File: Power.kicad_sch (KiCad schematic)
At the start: 54 parts, among them IC115 RC4558, IC116 RC4558, IC117 RC4558, IC118 L7805, IC121 1951A, IC135 74HC86, IC136 1951A, P1 Conn_01x02_Male, P3 Conn_01x02_Male

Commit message: PCE expansion port added with only relevant pins.
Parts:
- removed R120: 270, symbol Device:R
- added SPC-E: PCE-EXPANSION-CONN, symbol IFU-30:PCE-EXPANSION-CONN
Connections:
- net 8.5V: now also SPC-E.A11 (VIN), SPC-E.A14 (VIN)
- net GND: now also SPC-E.A21 (GNDA), SPC-E.B2 (CDD), SPC-E.C17 (GNDD), SPC-E.C2 (GNDA), SPC-E.C20 (GNDD), SPC-E.C8 (GNDD)
- net SPC-E_5V renamed PCE_5VOUT
- net PCE_5VOUT: now also SPC-E.A2 (VOUT), SPC-E.C21 (VOUT)
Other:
- moved on the sheet: C1, C103, C132, C133, C134, C15, C2, C3, C54, C55, C6, C7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

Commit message: All calculations added.
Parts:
- added IC114: TL072, symbol Amplifier_Operational:TL072
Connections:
- net 7.9V: now also IC114.8 (V+)
- net GND: now also IC114.4 (V-)
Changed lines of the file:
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@@
+    (stroke (width 0) (type default) (color 0 0 0 0))
+  )
+  (wire (pts (xy 329.565 238.125) (xy 329.565 239.395))
     (stroke (width 0) (type default) (color 0 0 0 0))
   )
@@
     (stroke (width 0) (type default) (color 0 0 0 0))
   )
+  (wire (pts (xy 329.565 222.25) (xy 321.945 222.25))
+    (stroke (width 0) (type default) (color 0 0 0 0))
+  )
   (wire (pts (xy 127 102.87) (xy 113.665 102.87))
     (stroke (width 0) (type default) (color 0 0 0 0))
@@
   )
   (wire (pts (xy 243.84 211.455) (xy 252.73 211.455))
+    (stroke (width 0) (type default) (color 0 0 0 0))
+  )
+  (wire (pts (xy 329.565 222.25) (xy 329.565 222.885))
     (stroke (width 0) (type default) (color 0 0 0 0))
   )
@@
   )
   (label "8.5V" (at 64.77 128.27 0)
+    (effects (font (size 1.27 1.27)) (justify left bottom))
+  )
+  (label "7.9V" (at 321.945 222.25 0)
     (effects (font (size 1.27 1.27)) (justify left bottom))
   )
@@
     (pin "1")
   )
+  (symbol (lib_id "Amplifier_Operational:TL072") (at 332.105 230.505 0) (unit 3)
+    (in_bom yes) (on_board yes) (fields_autoplaced)
+    (property "Reference" "IC114" (id 0) (at 330.2 229.6703 0)
+      (effects (font (size 1.27 1.27)) (justify left))
+    )
+    (property "Value" "TL072" (id 1) (at 330.2 232.2072 0)
+      (effects (font (size 1.27 1.27)) (justify left))
+    )
+    (property "Footprint" "" (id 2) (at 332.105 230.505 0)
+      (effects (font (size 1.27 1.27)) hide)
+    )
+    (property "Datasheet" "http://www.ti.com/lit/ds/symlink/tl071.pdf" (id 3) (at 332.105 230.505 0)
+      (effects (font (size 1.27 1.27)) hide)
+    )
+    (pin "1")
+    (pin "2")
+    (pin "3")
+    (pin "5")
+    (pin "6")
+    (pin "7")
+    (pin "4")
+    (pin "8")
+  )
   (symbol (lib_id "74xx:74HC86") (at 207.645 211.455 0) (unit 2)
     (in_bom yes) (on_board yes) (fields_autoplaced)
@@
       (effects (font (size 1.27 1.27)) hide)
     )
+    (pin "1")
+  )
+  (symbol (lib_id "power:GND") (at 329.565 239.395 0) (mirror y) (unit 1)
+    (in_bom yes) (on_board yes)
+    (property "Reference" "#PWR0102" (id 0) (at 329.565 245.745 0)
+      (effects (font (size 1.27 1.27)) hide)
+    )
+    (property "Value" "GND" (id 1) (at 329.565 243.84 0))
+    (property "Footprint" "" (id 2) (at 329.565 239.395 0)
+      (effects (font (size 1.27 1.27)) hide)
+    )
+    (property "Datasheet" "" (id 3) (at 329.565 239.395 0)
+      (effects (font (size 1.27 1.27)) hide)
+    )

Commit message: Documentation started.
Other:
- title: (none) -> NEC PC-Engine IFU-30
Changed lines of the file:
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@@
 (kicad_sch (version 20211123) (generator eeschema)
   (paper "A3")
+  (title_block
+    (title "NEC PC-Engine IFU-30")
+    (date "2022-10-27")
+    (rev "0.1")
+    (comment 1 "Author: Regis Galland")
+    (comment 2 "NEC IFU-30 PCB reverse engineered schematics")
+  )
   (junction (at 163.195 128.27) (diameter 0) (color 0 0 0 0)
   )

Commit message: Documentation update
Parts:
- ZD10: value D_Zener -> 5.1V
- ZD11: value D_Zener -> 8.2V
- renumbered SPC-E to SPC-E1
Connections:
- net 7.9V renamed 7.8V
- net VBIAS_3.95V renamed VBIAS_3.9V
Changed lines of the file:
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@@
     (effects (font (size 1.27 1.27)) (justify left bottom))
   )
-  (label "7.9V" (at 321.945 222.25 0)
+  (label "7.8V" (at 321.945 222.25 0)
     (effects (font (size 1.27 1.27)) (justify left bottom))
   )
@@
     (effects (font (size 1.27 1.27)) (justify left bottom))
   )
-  (label "VBIAS_3.95V" (at 168.91 105.41 0)
+  (label "VBIAS_3.9V" (at 168.91 105.41 0)
     (effects (font (size 1.27 1.27)) (justify left bottom))
   )
-  (label "7.9V" (at 100.33 89.535 0)
+  (label "7.8V" (at 100.33 89.535 0)
     (effects (font (size 1.27 1.27)) (justify left bottom))
   )
-  (hierarchical_label "7.9V" (shape output) (at 102.87 85.09 0)
+  (hierarchical_label "7.8V" (shape output) (at 102.87 85.09 0)
     (effects (font (size 1.27 1.27)) (justify left))
   )
@@
     (effects (font (size 1.27 1.27)) (justify left))
   )
-  (hierarchical_label "VBIAS_3.95V" (shape output) (at 200.025 105.41 0)
+  (hierarchical_label "VBIAS_3.9V" (shape output) (at 200.025 105.41 0)
     (effects (font (size 1.27 1.27)) (justify left))
   )
@@
     (pin "2")
   )
-  (symbol (lib_id "IFU-30:PCE-EXPANSION-CONN") (at 74.93 127 0) (unit 4)
-    (in_bom yes) (on_board yes)
-    (property "Reference" "SPC-E" (id 0) (at 90.17 121.2881 0))
-    (property "Value" "PCE-EXPANSION-CONN" (id 1) (at 90.17 123.825 0))
-    (property "Footprint" "" (id 2) (at 74.93 127 0)
-      (effects (font (size 1.27 1.27)) hide)
-    )
-    (property "Datasheet" "" (id 3) (at 74.93 127 0)
+  (symbol (lib_id "IFU-30:PCE-EXPANSION-CONN") (at 74.93 128.27 0) (unit 4)
+    (in_bom yes) (on_board yes)
+    (property "Reference" "SPC-E1" (id 0) (at 90.17 122.5581 0))
+    (property "Value" "PCE-EXPANSION-CONN" (id 1) (at 90.17 125.095 0))
+    (property "Footprint" "" (id 2) (at 74.93 128.27 0)
+      (effects (font (size 1.27 1.27)) hide)
+    )
+    (property "Datasheet" "" (id 3) (at 74.93 128.27 0)
       (effects (font (size 1.27 1.27)) hide)
     )
@@
     (pin "1")
   )
+  (symbol (lib_id "power:GND") (at 365.125 45.085 0) (unit 1)
+    (in_bom yes) (on_board yes) (fields_autoplaced)
+    (property "Reference" "#PWR0224" (id 0) (at 365.125 51.435 0)
+      (effects (font (size 1.27 1.27)) hide)
+    )
+    (property "Value" "GND" (id 1) (at 365.125 49.5284 0))
+    (property "Footprint" "" (id 2) (at 365.125 45.085 0)
+      (effects (font (size 1.27 1.27)) hide)
+    )
+    (property "Datasheet" "" (id 3) (at 365.125 45.085 0)
+      (effects (font (size 1.27 1.27)) hide)
+    )
+    (pin "1")
+  )
   (symbol (lib_id "power:GND") (at 360.045 147.32 90) (unit 1)
     (in_bom yes) (on_board yes) (fields_autoplaced)
@@
   (symbol (lib_id "Device:Q_PNP_ECB") (at 274.955 103.505 180) (unit 1)
     (in_bom yes) (on_board yes)
-    (property "Reference" "TR1" (id 0) (at 266.7031 95.885 90)
-      (effects (font (size 1.27 1.27)) (justify left))
-    )
-    (property "Value" "Q_PNP_ECB" (id 1) (at 269.24 95.885 90)
+    (property "Reference" "TR1" (id 0) (at 269.24 104.1369 0)
+      (effects (font (size 1.27 1.27)) (justify left))
+    )
+    (property "Value" "Q_PNP_ECB" (id 1) (at 269.24 101.6 0)
       (effects (font (size 1.27 1.27)) (justify left))
     )
@@
   (symbol (lib_id "Device:R") (at 309.245 52.705 0) (mirror x) (unit 1)
     (in_bom yes) (on_board yes)
-    (property "Reference" "R105" (id 0) (at 313.9608 52.705 90))
-    (property "Value" "820" (id 1) (at 311.785 52.705 90))
+    (property "Reference" "R105" (id 0) (at 313.69 51.1642 0))
+    (property "Value" "820" (id 1) (at 313.69 53.34 0))
     (property "Footprint" "" (id 2) (at 307.467 52.705 90)
       (effects (font (size 1.27 1.27)) hide)
@@
   (symbol (lib_id "Device:D_Zener") (at 266.065 162.56 0) (mirror x) (unit 1)
     (in_bom yes) (on_board yes)
-    (property "Reference" "ZD13" (id 0) (at 265.2303 164.592 90)
-      (effects (font (size 1.27 1.27)) (justify left))
-    )
-    (property "Value" "D_Zener" (id 1) (at 267.7672 164.592 90)
+    (property "Reference" "ZD13" (id 0) (at 262.255 158.75 0)
+      (effects (font (size 1.27 1.27)) (justify left))
+    )
+    (property "Value" "D_Zener" (id 1) (at 262.255 156.2131 0)
       (effects (font (size 1.27 1.27)) (justify left))
     )
@@
   (symbol (lib_id "Device:D") (at 309.245 41.91 270) (mirror x) (unit 1)
     (in_bom yes) (on_board yes)
-    (property "Reference" "D8" (id 0) (at 311.785 41.91 0))
+    (property "Reference" "D8" (id 0) (at 313.055 40.64 90))
     (property "Value" "D" (id 1) (at 310.515 39.37 0)
       (effects (font (size 1.27 1.27)) hide)
@@
       (effects (font (size 1.27 1.27)) (justify left))
     )
-    (property "Value" "D_Zener" (id 1) (at 57.277 88.6972 90)
+    (property "Value" "8.2V" (id 1) (at 57.277 88.6972 90)
       (effects (font (size 1.27 1.27)) (justify left))
     )
@@
   (symbol (lib_id "Device:D") (at 203.835 45.72 90) (unit 1)
     (in_bom yes) (on_board yes)
-    (property "Reference" "D1" (id 0) (at 201.295 45.72 0))
+    (property "Reference" "D1" (id 0) (at 207.645 45.085 90))
     (property "Value" "D" (id 1) (at 202.565 43.18 0)
       (effects (font (size 1.27 1.27)) hide)
@@
       (effects (font (size 1.27 1.27)) (justify left))
     )
-    (property "Value" "D_Zener" (id 1) (at 307.213 105.8422 90)
+    (property "Value" "5.1V" (id 1) (at 307.213 105.8422 90)
       (effects (font (size 1.27 1.27)) (justify left))
     )
@@
     (pin "1")
   )
+  (symbol (lib_id "power:PWR_FLAG") (at 365.125 45.085 0) (unit 1)
+    (in_bom yes) (on_board yes) (fields_autoplaced)
+    (property "Reference" "#FLG0106" (id 0) (at 365.125 43.18 0)
+      (effects (font (size 1.27 1.27)) hide)
+    )
+    (property "Value" "PWR_FLAG" (id 1) (at 365.125 41.5092 0))
+    (property "Footprint" "" (id 2) (at 365.125 45.085 0)
+      (effects (font (size 1.27 1.27)) hide)
+    )
+    (property "Datasheet" "~" (id 3) (at 365.125 45.085 0)
+      (effects (font (size 1.27 1.27)) hide)
+    )
+    (pin "1")
+  )
   (symbol (lib_id "Device:D") (at 255.905 162.56 0) (mirror y) (unit 1)
-    (in_bom yes) (on_board yes) (fields_autoplaced)
-    (property "Reference" "D16" (id 0) (at 256.7397 160.528 90)
-      (effects (font (size 1.27 1.27)) (justify left))
-    )
-    (property "Value" "D" (id 1) (at 254.2028 160.528 90)
+    (in_bom yes) (on_board yes)
+    (property "Reference" "D16" (id 0) (at 256.54 157.48 0)
+      (effects (font (size 1.27 1.27)) (justify left))
+    )
+    (property "Value" "D" (id 1) (at 256.54 160.0169 0)
       (effects (font (size 1.27 1.27)) (justify left))
     )
@@
   )
   (symbol (lib_id "Device:D") (at 221.615 211.455 180) (unit 1)
-    (in_bom yes) (on_board yes) (fields_autoplaced)
-    (property "Reference" "D11" (id 0) (at 220.7803 209.423 90)
-      (effects (font (size 1.27 1.27)) (justify right))
-    )
-    (property "Value" "D" (id 1) (at 223.3172 209.423 90)
+    (in_bom yes) (on_board yes)
+    (property "Reference" "D11" (id 0) (at 220.98 205.7431 0)
+      (effects (font (size 1.27 1.27)) (justify right))
+    )
+    (property "Value" "D" (id 1) (at 220.98 208.28 0)
       (effects (font (size 1.27 1.27)) (justify right))
     )
@@
   )
   (symbol (lib_id "Device:D") (at 221.615 179.705 180) (unit 1)
-    (in_bom yes) (on_board yes) (fields_autoplaced)
-    (property "Reference" "D12" (id 0) (at 220.7803 177.673 90)
-      (effects (font (size 1.27 1.27)) (justify right))
-    )
-    (property "Value" "D" (id 1) (at 223.3172 177.673 90)
-      (effects (font (size 1.27 1.27)) (justify right))
-    )
+    (in_bom yes) (on_board yes)
+    (property "Reference" "D12" (id 0) (at 220.345 173.99 0)
+      (effects (font (size 1.27 1.27)) (justify right))
+    )
+    (property "Value" "D" (id 1) (at 220.345 176.5269 0)
+      (effects (font (size 1.27 1.27)) (justify right))
+    )

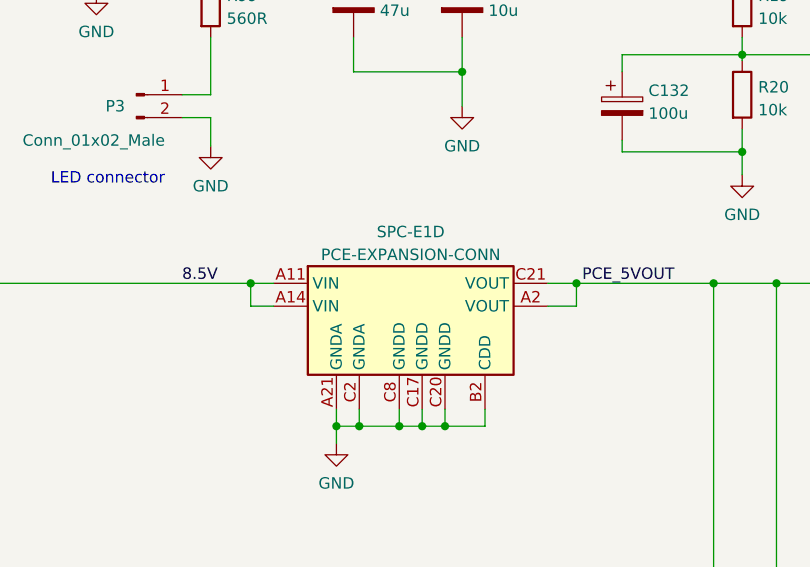
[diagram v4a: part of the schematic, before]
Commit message: Unsused pins from expansion conenctor on 1 page. CD conenctor signals added.
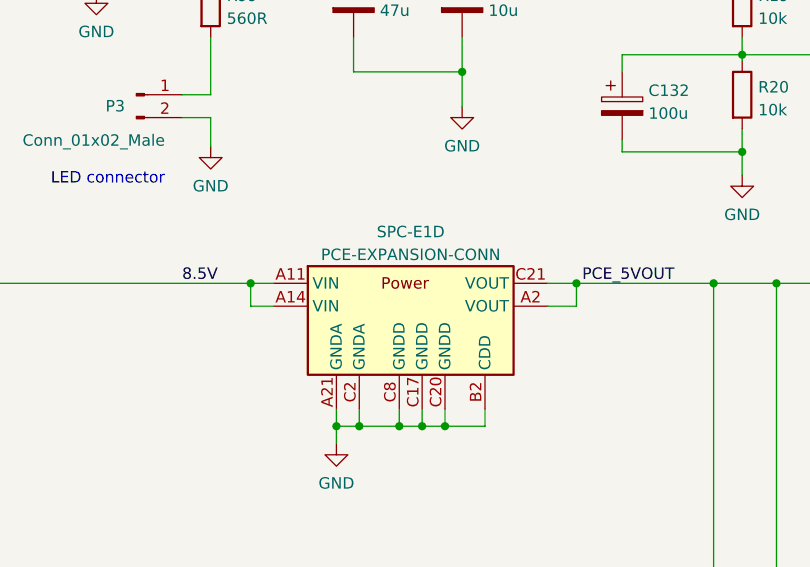
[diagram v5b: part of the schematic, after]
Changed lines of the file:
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@@
       (effects (font (size 1.27 1.27)) hide)
     )
-    (pin "A4")
-    (pin "A5")
+    (pin "A04")
+    (pin "A05")
     (pin "A6")
     (pin "A7")
@@
     (pin "B19")
     (pin "B6")
+    (pin "C05")
+    (pin "C06")
     (pin "C13")
     (pin "C14")
@@
     (pin "C18")
     (pin "C19")
-    (pin "C5")
-    (pin "C6")
     (pin "C7")
     (pin "A0")
@@
     (pin "C0")
     (pin "A8")
+    (pin "B02")
     (pin "B10")
     (pin "B21")
@@
     (pin "C21")
     (pin "C8")
+    (pin "A03")
+    (pin "A09")
+    (pin "A10")
+    (pin "A12")
+    (pin "A13")
+    (pin "A15")
+    (pin "A16")
+    (pin "A17")
+    (pin "A18")
+    (pin "A19")
+    (pin "A20")
+    (pin "A23")
+    (pin "B03")
+    (pin "B05")
+    (pin "B11")
+    (pin "B14")
+    (pin "B20")
+    (pin "B22")
+    (pin "B23")
+    (pin "C03")
+    (pin "C04")
+    (pin "C22")
+    (pin "C23")
   )
   (symbol (lib_id "power:GND") (at 243.84 224.155 0) (unit 1)

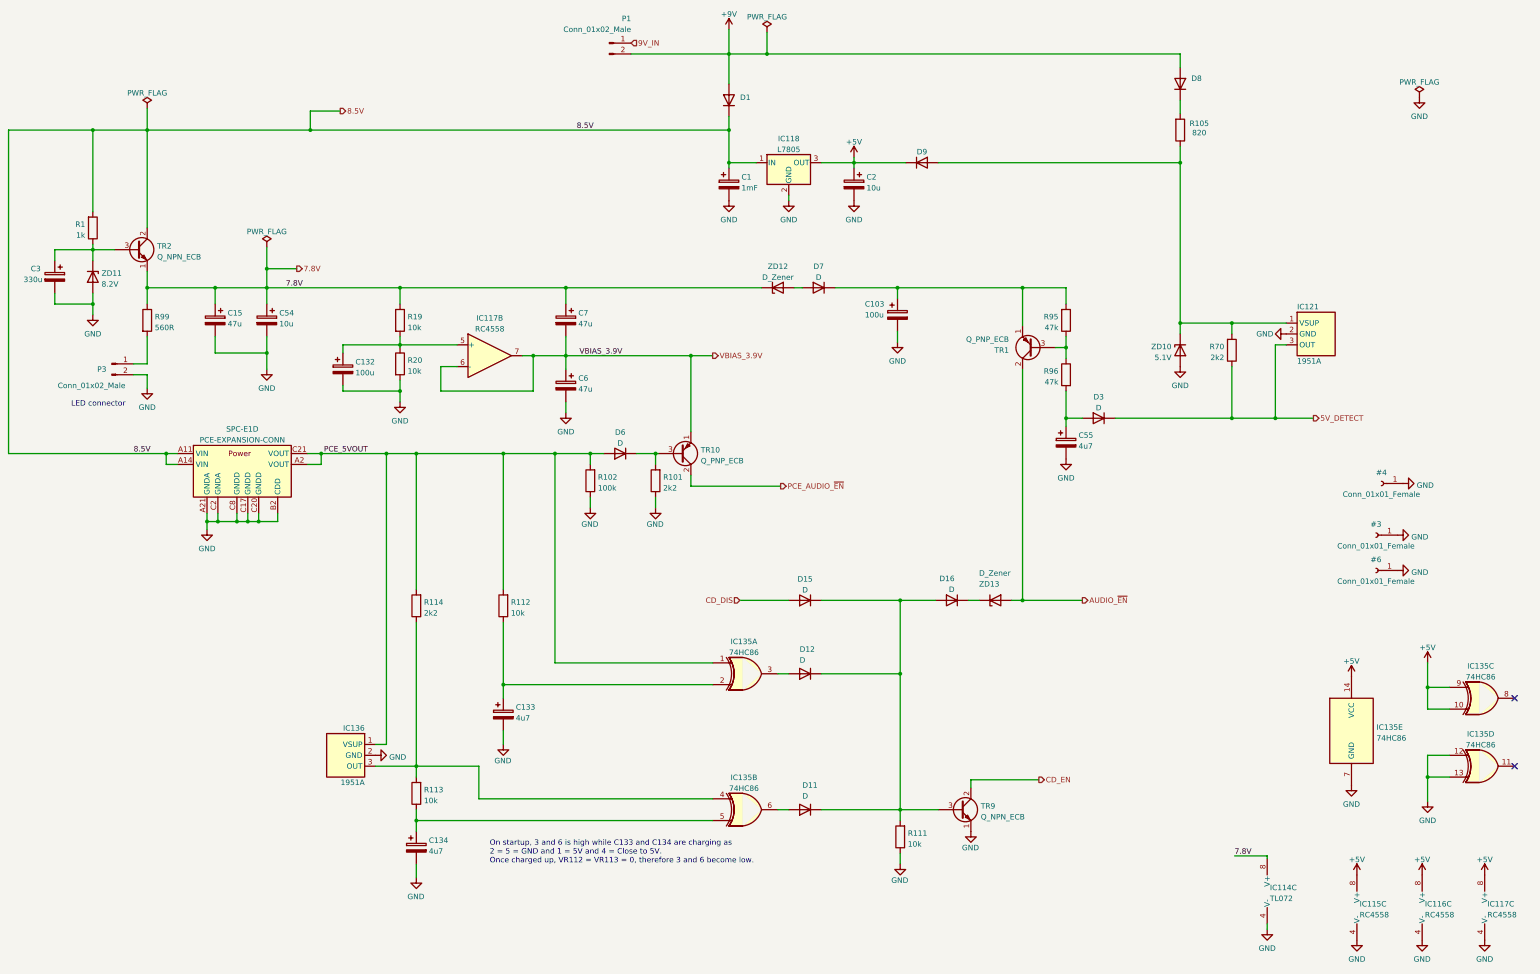
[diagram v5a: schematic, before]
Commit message: Fixed a few typos and mainly renamed connections to CD-ROM with more accurate descriptions
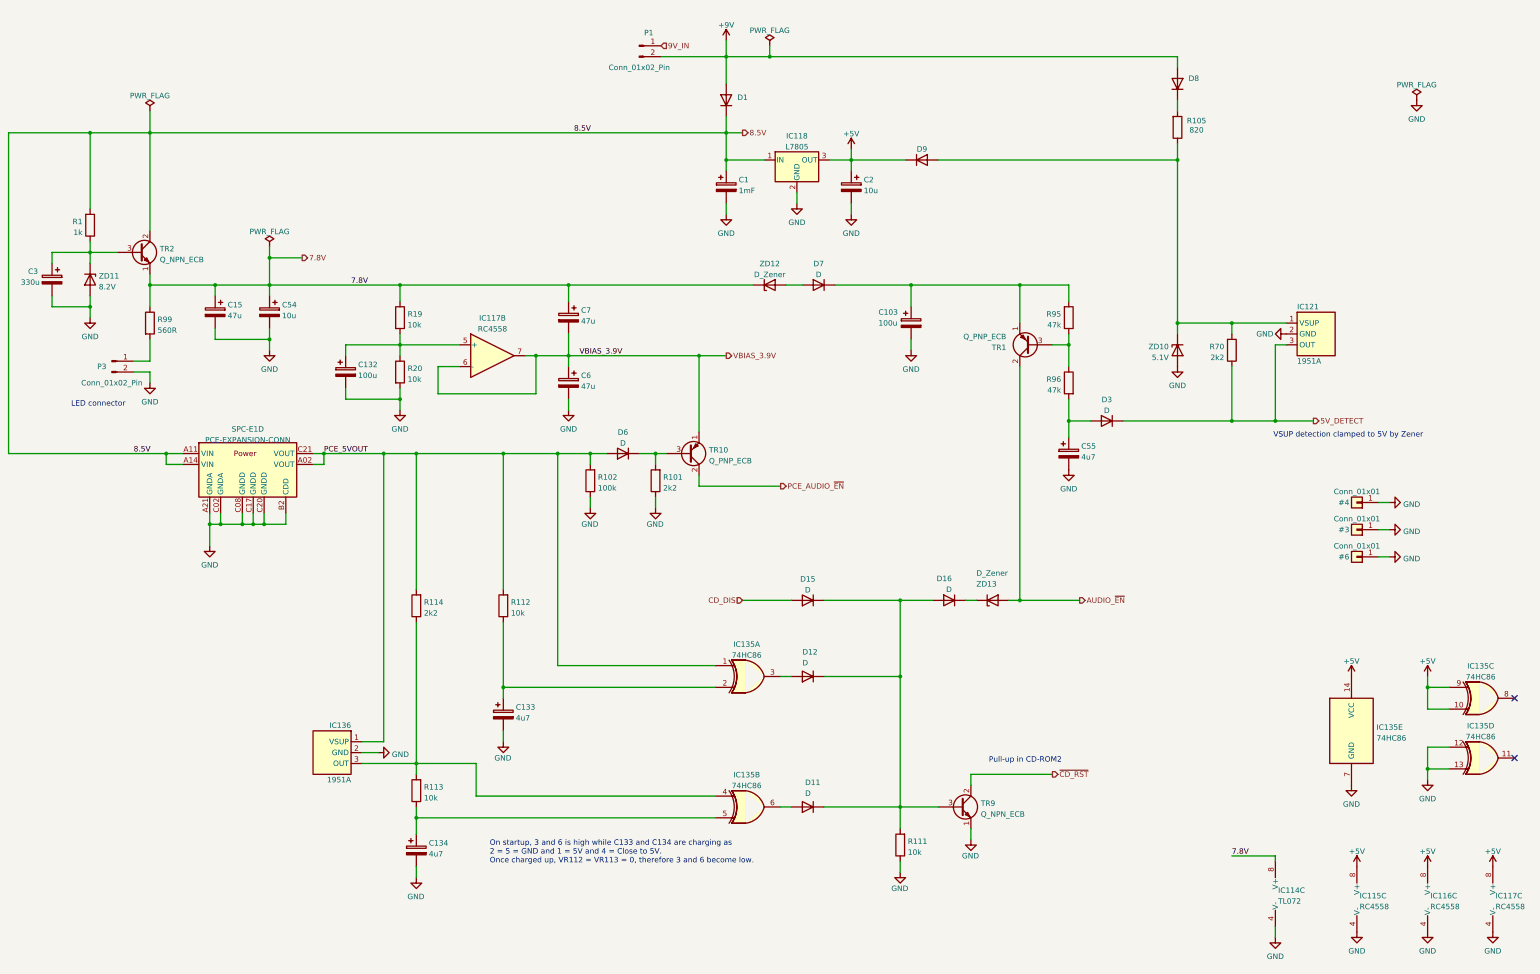
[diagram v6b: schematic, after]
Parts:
- P1, P3: value Conn_01x02_Male -> Conn_01x02_Pin; symbol Connector:Conn_01x02_Male -> Connector:Conn_01x02_Pin
- SPC-E1: footprint (none) -> IFU-30:PinSocket_3x23_P2.54mm_Horizontal
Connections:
- net GND: now also SPC-E1.C02 (GNDA), SPC-E1.C08 (GNDD); no longer SPC-E1.C2 (GNDA), SPC-E1.C8 (GNDD)
- net PCE_5VOUT: now also SPC-E1.A02 (VOUT); no longer SPC-E1.A2 (VOUT)
- net CD_EN renamed ~{CD_RST}
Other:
- note added: "Pull-up in CD-ROM2"
- note added: "VSUP detection clamped to 5V by Zener"
- moved on the sheet: C1, C103, C132, C134, C15, C2, C3, C54, C55, C6, C7, D1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
